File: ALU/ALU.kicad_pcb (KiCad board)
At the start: 2 copper layers, 85 x 99.5 mm, 19 parts

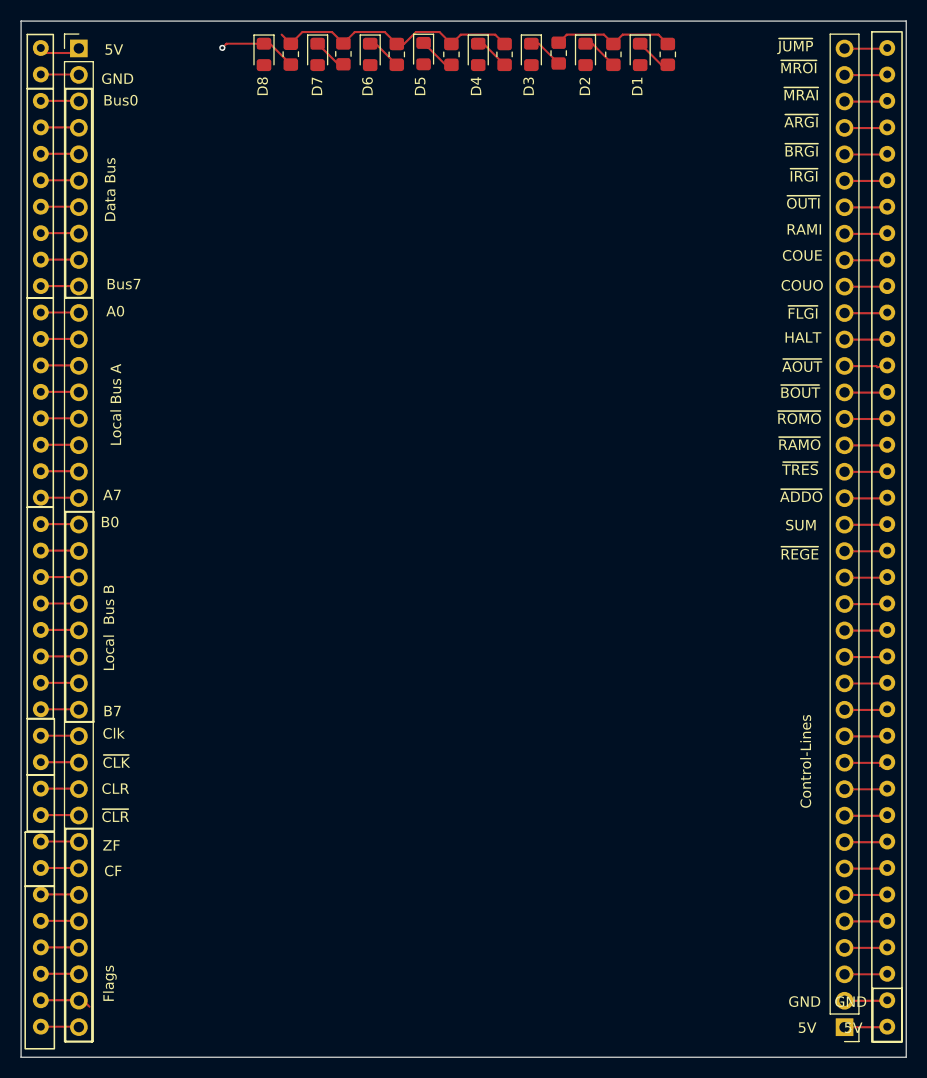
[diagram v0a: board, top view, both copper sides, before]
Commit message: [ALU] - First fully routed and reviewed version of the ALU.
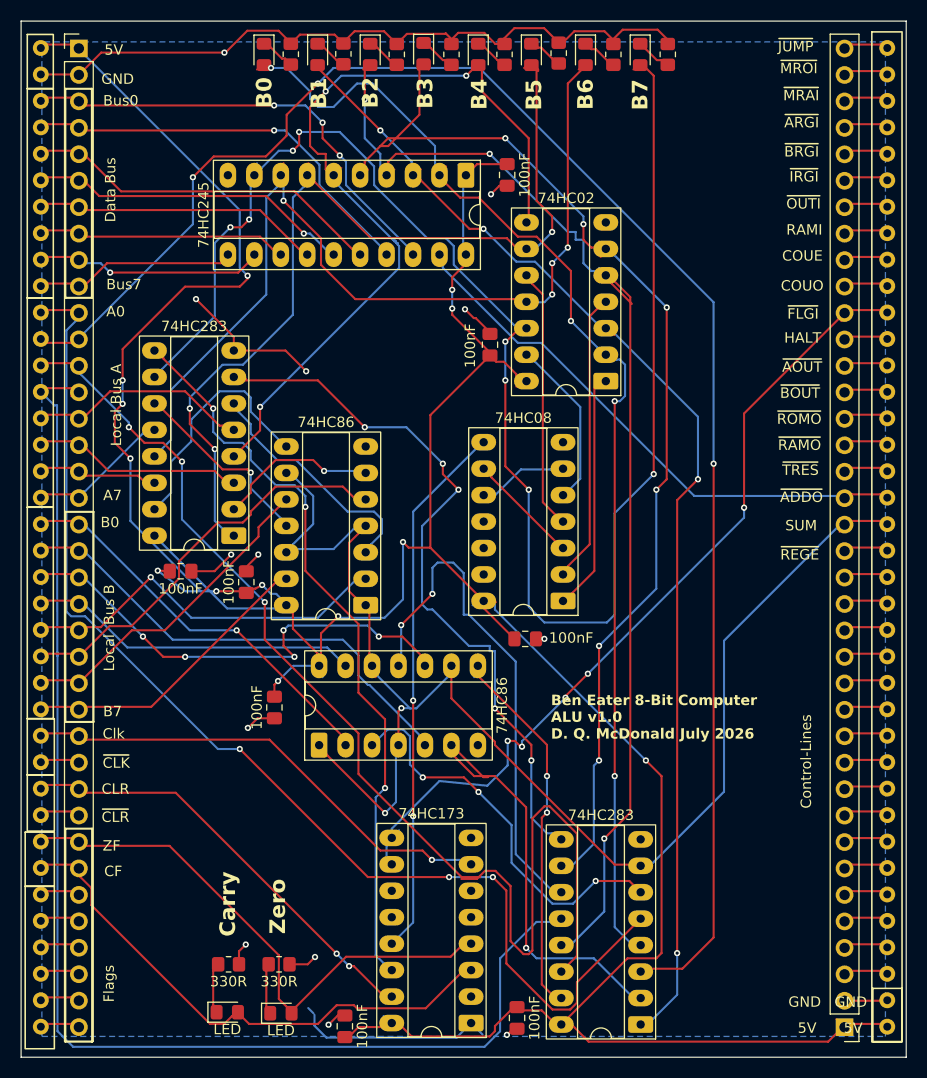
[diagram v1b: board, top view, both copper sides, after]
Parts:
- added C1: 100nF, Capacitor_SMD:C_0805_2012Metric_Pad1.18x1.45mm_HandSolder, F.Cu at (70.4, 43.5)
- added C2: 100nF, Capacitor_SMD:C_0805_2012Metric_Pad1.18x1.45mm_HandSolder, F.Cu at (39.0, 81.5)
- added C3: 100nF, Capacitor_SMD:C_0805_2012Metric_Pad1.18x1.45mm_HandSolder, F.Cu at (48.0, 94.6)
- added C4: 100nF, Capacitor_SMD:C_0805_2012Metric_Pad1.18x1.45mm_HandSolder, F.Cu at (71.3, 124.4)
- added C5: 100nF, Capacitor_SMD:C_0805_2012Metric_Pad1.18x1.45mm_HandSolder, F.Cu at (45.4, 82.5)
- added C7: 100nF, Capacitor_SMD:C_0805_2012Metric_Pad1.18x1.45mm_HandSolder, F.Cu at (54.8, 125.2)
- added C8: 100nF, Capacitor_SMD:C_0805_2012Metric_Pad1.18x1.45mm_HandSolder, F.Cu at (68.8, 59.8)
- added C9: 100nF, Capacitor_SMD:C_0805_2012Metric_Pad1.18x1.45mm_HandSolder, F.Cu at (72.1, 88.0)
- added D10: LED, LED_SMD:LED_0805_2012Metric_Pad1.15x1.40mm_HandSolder, F.Cu at (48.7, 124.0)
- added D9: LED, LED_SMD:LED_0805_2012Metric_Pad1.15x1.40mm_HandSolder, F.Cu at (43.5, 123.8)
- added R10: 330R, Resistor_SMD:R_0805_2012Metric_Pad1.20x1.40mm_HandSolder, F.Cu at (48.5, 119.2)
- added R9: 330R, Resistor_SMD:R_0805_2012Metric_Pad1.20x1.40mm_HandSolder, F.Cu at (43.6, 119.2)
- added U1: 74HC283, Package_DIP:DIP-16_W7.62mm_Socket_LongPads, F.Cu at (44.2, 78.1)
- added U2: 74HC283, Package_DIP:DIP-16_W7.62mm_Socket_LongPads, F.Cu at (83.2, 125.0)
- added U3: 74HC245, Package_DIP:DIP-20_W7.62mm_Socket_LongPads, F.Cu at (66.4, 43.5)
- added U4: 74HC86, Package_DIP:DIP-14_W7.62mm_Socket_LongPads, F.Cu at (56.8, 84.8)
- added U5: 74HC86, Package_DIP:DIP-14_W7.62mm_Socket_LongPads, F.Cu at (52.3, 98.2)
- added U6: 74HC02, Package_DIP:DIP-14_W7.62mm_Socket_LongPads, F.Cu at (79.9, 63.3)
- added U7: 74HC08, Package_DIP:DIP-14_W7.62mm_Socket_LongPads, F.Cu at (75.8, 84.4)
- added U8: 74HC173, Package_DIP:DIP-16_W7.62mm_Socket_LongPads, F.Cu at (66.9, 124.9)
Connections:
- net ZFLG renamed ZFLAG
- D1 pad 2: unconnected-(D1-A-Pad2) -> SUM7
- D2 pad 2: unconnected-(D2-A-Pad2) -> SUM6
- D3 pad 2: unconnected-(D3-A-Pad2) -> SUM5
- D4 pad 2: unconnected-(D4-A-Pad2) -> SUM4
- D5 pad 2: unconnected-(D5-A-Pad2) -> SUM3
- D6 pad 2: unconnected-(D6-A-Pad2) -> SUM2
- D7 pad 2: unconnected-(D7-A-Pad2) -> SUM1
- D8 pad 2: unconnected-(D8-A-Pad2) -> SUM0
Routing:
- net 5V: track 9.15 -> 325.2 mm, vias 0 -> 13
- net SUM7: track 0.00 -> 158.2 mm, vias 0 -> 8
- net LBA1: track 3.90 -> 159.1 mm, vias 0 -> 3
- net SUB: track 3.80 -> 144.6 mm, vias 0 -> 2
- net LBA3: track 3.90 -> 126.3 mm
- net SUM2: track 0.00 -> 115.8 mm, vias 0 -> 3
- net SUM1: track 0.00 -> 114.7 mm, vias 0 -> 4
- net SUM0: track 0.00 -> 114.2 mm, vias 0 -> 4
- net LBA2: track 3.90 -> 117.0 mm, vias 0 -> 3
- net SUM3: track 0.00 -> 112.0 mm, vias 0 -> 6
- net LBA0: track 3.90 -> 112.7 mm, vias 0 -> 3
- net SUM6: track 0.00 -> 91.2 mm, vias 0 -> 4
- net SUM5: track 0.00 -> 89.0 mm, vias 0 -> 3
- net GND: track 45.3 -> 131.7 mm, vias 0 -> 13
- net SUM4: track 0.00 -> 82.6 mm, vias 0 -> 3
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- added copper zone on B.Cu, net GND
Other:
- board text added: "B0"
- board text added: "B1"
- board text added: "B2"
- board text added: "B3"
- board text added: "B4"
- board text added: "B5"
- board text added: "B6"
- board text added: "B7"
- board text added: "Ben Eater 8-Bit Computer ALU v1.0 D. Q. McDonald July 2026"
- board text added: "Carry"
- board text added: "Zero"
